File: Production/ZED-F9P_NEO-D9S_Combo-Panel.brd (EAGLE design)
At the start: 43.2 x 63.5 mm, 179 parts, among them J1 ANTENNA-SMA-GROUNDEDEDGE_SMA, J2 Qwiic Right Angle, J4 Qwiic Right Angle, U1 U-BLOX_NEO-D9S-00B, U2 3.3V, U4 U-BLOX_ZED-F9P, U5 ESD Diode, U6 ESD Diode, U7 BP2G1+_POWER_SPLITTER

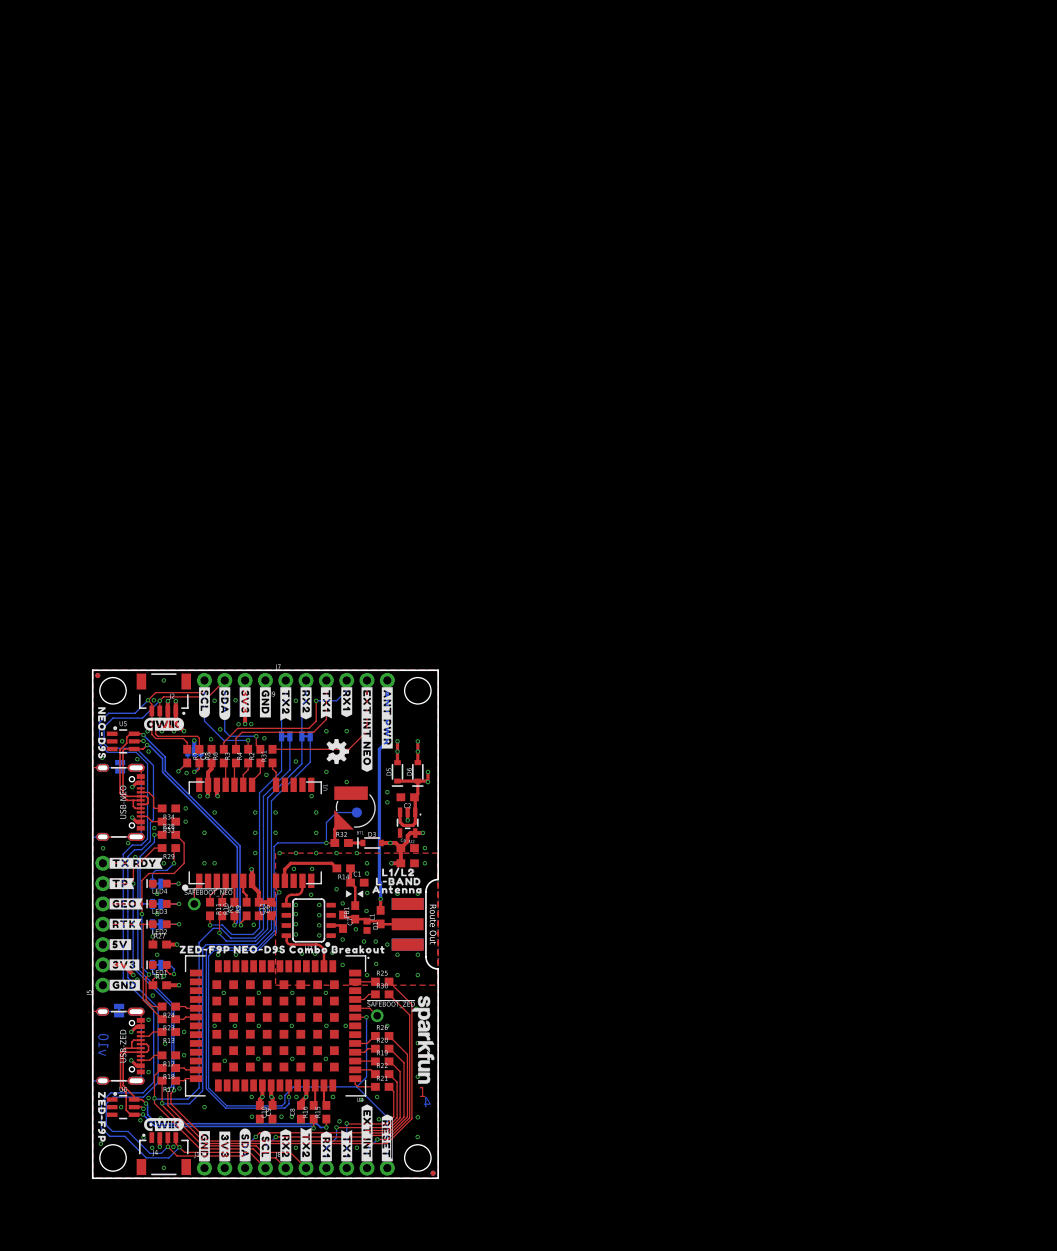
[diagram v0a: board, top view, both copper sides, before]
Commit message: Adds new panel
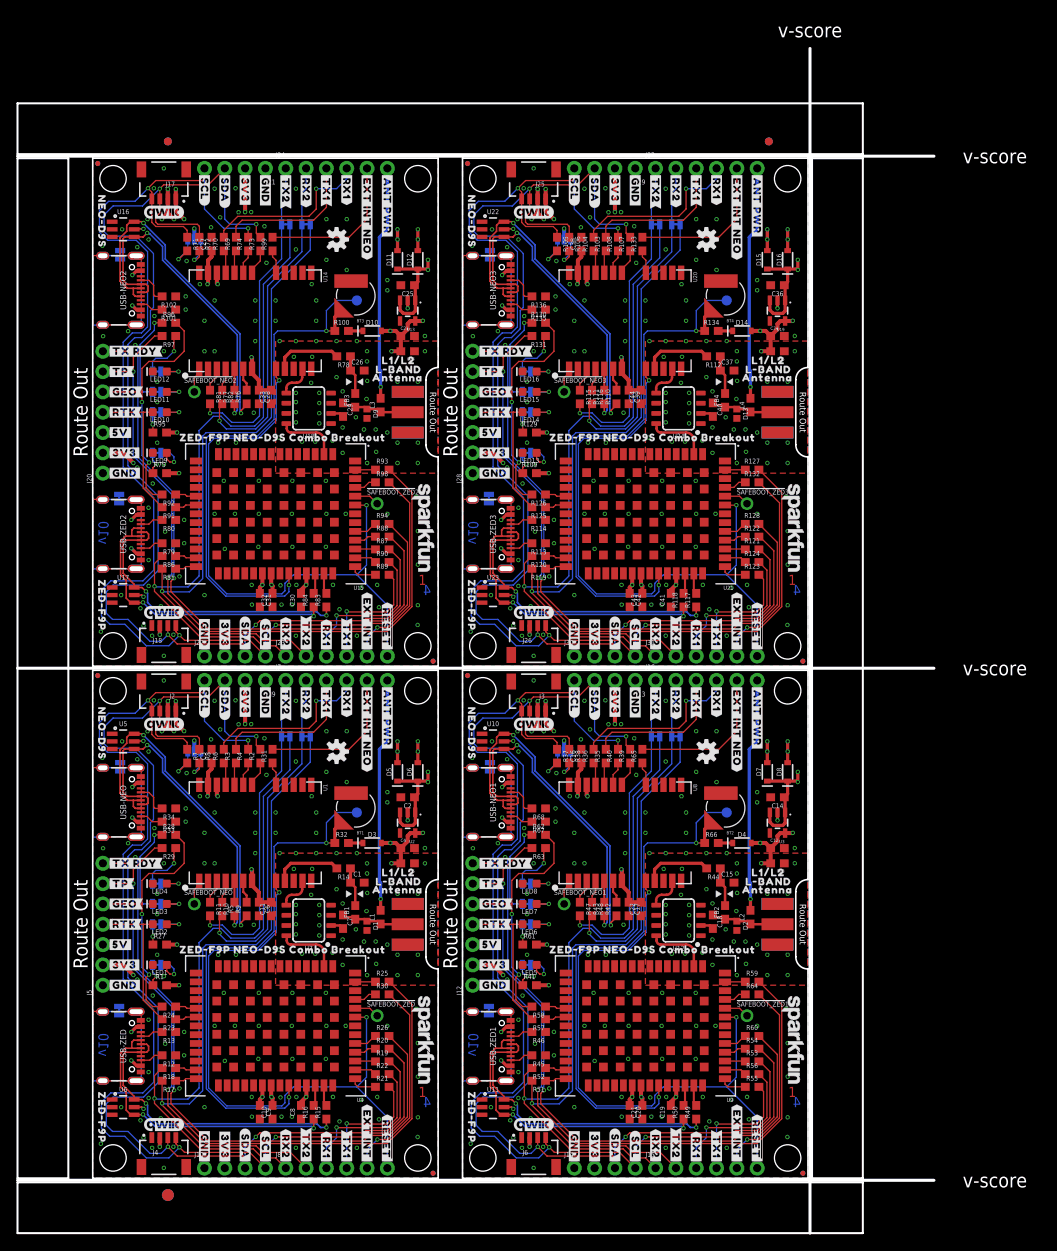
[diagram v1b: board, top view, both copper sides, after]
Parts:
- removed FRAME2: FRAME-LEDGER, SparkFun-Aesthetics:CREATIVE_COMMONS
- added !SAFEBOOT_NEO!1, !SAFEBOOT_NEO!2, !SAFEBOOT_NEO!3, !SAFEBOOT_ZED!1, !SAFEBOOT_ZED!2, !SAFEBOOT_ZED!3: TEST-POINTPOGO_PTH, SparkFun-Connectors:1X01_NO_SILK
- added BT2, BT3, BT4: RELOWABLE_BATTERY_MS421R, SparkFun-Batteries:MS421R_IV03E
- added C12, C14, C16, C17, C19, C20, C23, C25, C27, C28, C30, C31, C34, C36, C38, C39, C41, C42: 1.0uF, SparkFun-Capacitors:0603
- added C13, C21, C22, C24, C32, C33, C35, C43, C44: 0.1uF, SparkFun-Capacitors:0603
- added C15, C18, C26, C29, C37, C40: 47pF, SparkFun-Capacitors:0603
- added D10, D14, D4: 0.5A/40V/420mV, SparkFun-DiscreteSemi:SOD-323
- added D11, D12, D15, D16, D7, D8: 1A/23V/620mV, SparkFun-DiscreteSemi:SOD-323
- added D13, D2, D9: PESD0402-0402, SparkFun-DiscreteSemi:0402
- added E$1, E$2, E$3, E$4: (no value), SparkFun-Aesthetics:FIDUCIAL-1X2
- added E$5, E$6: (no value), SparkFun-Retired:FIDUCIAL-1.5X3
- added FB2, FB3, FB4: 30Ω/1.8A, SparkFun-Coils:0603
- added GEO1, GEO2, GEO3, PWR\1, PWR\2, PWR\3, RTK1, RTK2, RTK3, RX2-TX1, RX2-TX3, RX2-TX4, SHLD_NEO1, SHLD_NEO2, SHLD_NEO3, SHLD_ZED1, SHLD_ZED2, SHLD_ZED3, TP1, TP2, TP3, TX2-RX1, TX2-RX3, TX2-RX4: JUMPER-SMT_2_NC_TRACE_SILK, SparkFun-Jumpers:SMT-JUMPER_2_NC_TRACE_SILK
- added I2C1, I2C2, I2C3: JUMPER-SMT_3_NO_SILK, SparkFun-Jumpers:SMT-JUMPER_3_NO_SILK
- added J11, J19, J27: ANTENNA-SMA-GROUNDEDEDGE_SMA, SparkFun-RF:SMA-EDGE
- added J12, J20, J28: (no value), SparkFun-Connectors:1X07_NO_SILK
- added J13, J14, J21, J22, J29, J30: (no value), SparkFun-Connectors:1X04_NO_SILK
- added J15, J16, J23, J24, J31, J32: (no value), SparkFun-Connectors:1X06_NO_SILK
- added J17, J18, J25, J26, J3, J6: Qwiic Right Angle, SparkFun-Connectors:JST04_1MM_RA
- added JP1, JP10, JP15, JP16, JP17, JP18, JP2, JP24, JP25, JP7, JP8, JP9: STAND-OFF, SparkFun:STAND-OFF
- added JP11, JP12, JP13, JP14, JP19, JP20, JP22, JP23, JP3, JP4, JP5, JP6: FIDUCIALUFIDUCIAL, SparkFun:MICRO-FIDUCIAL
- added L2, L3, L4: DNP, SparkFun-Coils:0603_NO-CREAM
- added LED10, LED11, LED12, LED14, LED15, LED16, LED6, LED7, LED8: BLUE, SparkFun-LED:LED-0603
- added LED13, LED5, LED9: RED, SparkFun-LED:LED-0603
- added LOGO10, LOGO14, LOGO15, LOGO19, LOGO20, LOGO9: QWIIC_LOGO_5MM, SparkFun-Aesthetics:QWIIC_5MM
- added LOGO11, LOGO12, LOGO16, LOGO17, LOGO7: OSHW-LOGOS, SparkFun-Aesthetics:OSHW-LOGO-S
- added LOGO13, LOGO18, LOGO8: SFE_LOGO_NAME.1_INCH, SparkFun-Aesthetics:SFE_LOGO_NAME_.1
- added R100, R134, R66: 3.3k, SparkFun-Resistors:0603
- added R101, R102, R113, R114, R135, R136, R45, R46, R67, R68, R79, R80: 5.1k, SparkFun-Resistors:0603
- added R103, R104, R107, R108, R115, R116, R119, R120, R121, R122, R123, R124, R125, R126, R127, R128, R132, R133, R35, R36, R39, R40, R47, R48, R51, R52, R53, R54, R55, R56, R57, R58, R59, R60, R64, R65, R69, R70, R73, R74, R81, R82, R85, R86, R87, R88, R89, R90, R91, R92, R93, R94, R98, R99: 33, SparkFun-Resistors:0603
- added R105, R106, R37, R38, R71, R72: 2.2k, SparkFun-Resistors:0603
- added R109, R41, R75: 4.7k, SparkFun-Resistors:0603
- added R110, R111, R117, R118, R42, R43, R49, R50, R76, R77, R83, R84: 27, SparkFun-Resistors:0603
- added R112, R44, R78: 10, SparkFun-Resistors:0603
- added R129, R130, R131, R61, R62, R63, R95, R96, R97: 1k, SparkFun-Resistors:0603
- added U$100, U$180, U$260: (no value), output:#RTK#0
- added U$101, U$181, U$261: (no value), output:#RTK#1
- added U$102, U$182, U$262: (no value), output:#GEO#0
- added U$103, U$183, U$263: (no value), output:#GEO#1
- added U$104, U$184, U$264: (no value), output:#TP#0
- added U$105, U$185, U$265: (no value), output:#TP#1
- added U$106, U$186, U$266: (no value), output:#TX_RDY#0
- added U$107, U$187, U$267: (no value), output:#TX_RDY#1
- added U$108, U$109, U$135, U$188, U$189, U$215, U$268, U$269, U$295: (no value), output:#RX2#0
- added U$110, U$111, U$190, U$191, U$270, U$271: (no value), output:#RX2#3
- added U$112, U$113, U$134, U$192, U$193, U$214, U$272, U$273, U$294: (no value), output:#TX2#0
- added U$114, U$115, U$194, U$195, U$274, U$275: (no value), output:#TX2#3
- added U$116, U$117, U$196, U$197, U$276, U$277: (no value), output:#RX1#0
- added U$118, U$119, U$198, U$199, U$278, U$279: (no value), output:#RX1#2
- added U$120, U$121, U$200, U$201, U$280, U$281: (no value), output:#TX1#0
- added U$122, U$123, U$202, U$203, U$282, U$283: (no value), output:#TX1#2
- added U$124, U$204, U$284: (no value), output:#EXT_INT_NEO#0
- added U$125, U$205, U$285: (no value), output:#EXT_INT_NEO#1
- added U$126, U$127, U$206, U$207, U$286, U$287: (no value), output:#SDA#0
- added U$128, U$129, U$208, U$209, U$288, U$289: (no value), output:#SDA#1
- added U$130, U$131, U$210, U$211, U$290, U$291: (no value), output:#SCL#0
- added U$132, U$133, U$212, U$213, U$292, U$293: (no value), output:#SCL#1
- added U$136, U$216, U$296: (no value), output:ZED#F9P10
- added U$137, U$217, U$297: (no value), output:NEO#D9S10
- added U$138, U$218, U$298: (no value), output:#PWR#0
- added U$139, U$171, U$172, U$219, U$251, U$252, U$299, U$91, U$92: (no value), output:#3V3#4
- added U$140, U$220, U$300: (no value), output:#EXT_INT_ZED#0
- added U$141, U$221, U$301: (no value), output:ZED#F9P_NEO#D9S_COMBO_BREAKOUT0
- added U$142, U$222, U$302: (no value), top:##SAFEBOOT#_NEO#13
- added U$143, U$223, U$303: (no value), top:##SAFEBOOT#_ZED#14
- added U$144, U$224, U$304: (no value), top:#SHLD_ZED#15
- added U$145, U$225, U$305: (no value), top:#SHLD_NEO#12
- added U$146, U$226, U$306: (no value), top:ZED#F9P16
- added U$147, U$227, U$307: (no value), top:NEO#D9S16
- added U$148, U$228, U$308: (no value), top:COMBO16
- added U$149, U$229, U$309: (no value), top:BREAKOUT17
- added U$150, U$230, U$310: (no value), SparkFun-Aesthetics:SFE_LOGO_NAME_.2
- added U$151, U$231, U$311: (no value), top:L1#L218
- added U$152, U$232, U$312: (no value), top:ANTENNA18
- added U$153, U$233, U$313: (no value), top:L#BAND18
- added U$154, U$234, U$314: (no value), top:OPEN_JUMPERS13
- added U$155, U$235, U$315: (no value), top:TO_ISOLATE_UART214
- added U$156, U$236, U$316: (no value), top:DEF_ADDRESS#_12
- added U$157, U$237, U$317: (no value), top:NEO#D9S#13
- added U$158, U$238, U$318: (no value), top:ZED#F9P#13
- added U$159, U$239, U$319: (no value), top:0X4313
- added U$160, U$240, U$320: (no value), top:0X4213
- added U$161, U$162, U$163, U$241, U$242, U$243, U$38, U$77, U$83: (no value), output:#GND#0
- added U$164, U$165, U$166, U$244, U$245, U$246, U$84, U$85, U$86: (no value), output:#GND#1
- added U$167, U$247, U$87: (no value), output:#5V#0
- added U$168, U$248, U$88: (no value), output:#5V#6
- added U$169, U$170, U$177, U$249, U$250, U$257, U$89, U$90, U$97: (no value), output:#3V3#0
- added U$173, U$253, U$93: (no value), output:##RESET##0
- added U$174, U$254, U$94: (no value), output:##RESET##1
- added U$175, U$255, U$95: (no value), output:#EXT_INT#0
- added U$176, U$256, U$96: (no value), output:#I�C#0
- added U$178, U$258, U$98: (no value), output:#ANT_PWR#0
- added U$179, U$259, U$99: (no value), output:#ANT_PWR#1
- added U10, U11, U16, U17, U22, U23: ESD Diode, SparkFun-DiscreteSemi:SOT-23-6
- added U12, U18, U24: BP2G1+_POWER_SPLITTER, SparkFun-RF:XX21
- added U13, U19, U3: 3.3V, SparkFun-IC-Power:SOT23-5
- added U14, U20, U8: U-BLOX_NEO-D9S-00B, SparkFun-GPS:NEO-M9N/M8T/M8U/D9S
- added U15, U21, U9: U-BLOX_ZED-F9P, SparkFun-GPS:ZED-F9P
- added USB-NEO1, USB-NEO2, USB-NEO3, USB-ZED1, USB-ZED2, USB-ZED3: USB Female Type C Connector, SparkFun-Connectors:USB-C-16P_4LAYER-PADS
- added V_BKCP1, V_BKCP2, V_BKCP3: TEST-POINT3X5, SparkFun-Connectors:PAD.03X.05
- LOGO5: value SPECIAL_INSTRUCTIONS-ORDERING -> OSHW-LOGOS; device SparkFun-Aesthetics:ORDERING_INSTRUCTIONS -> SparkFun-Aesthetics:OSHW-LOGO-S
- moved LOGO5 61.0 mm to (52.3, 2.54), flipped to the bottom, turned to 90 degrees
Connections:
- new net !RESET!1: J15.6, U8.8, U9.49
- new net !RESET!2: J23.6, U14.8, U15.49
- new net !RESET!3: J31.6, U20.8, U21.49
- new net !SAFEBOOT_NEO!1: !SAFEBOOT_NEO!1.1, U8.1
- new net !SAFEBOOT_NEO!2: !SAFEBOOT_NEO!2.1, U14.1
- new net !SAFEBOOT_NEO!3: !SAFEBOOT_NEO!3.1, U20.1
- new net !SAFEBOOT_ZED!1: !SAFEBOOT_ZED!1.1, U9.50
- new net !SAFEBOOT_ZED!2: !SAFEBOOT_ZED!2.1, U15.50
- new net !SAFEBOOT_ZED!3: !SAFEBOOT_ZED!3.1, U21.50
- new net 3.3V1: C12.1, C13.2, C16.1, C17.1, C19.2, C20.1, C21.2, C22.2, D4.A, I2C1.2, J12.2, J13.2, J14.2, J3.2, J6.2, R41.2, R61.2, U3.5, U8.22, U8.23, U8.7, U9.33, U9.34, U9.38
- new net 3.3V2: C23.1, C24.2, C27.1, C28.1, C30.2, C31.1, C32.2, C33.2, D10.A, I2C2.2, J17.2, J18.2, J20.2, J21.2, J22.2, R75.2, R95.2, U13.5, U14.22, U14.23, U14.7, U15.33, U15.34, U15.38
- new net 3.3V3: C34.1, C35.2, C38.1, C39.1, C41.2, C42.1, C43.2, C44.2, D14.A, I2C3.2, J25.2, J26.2, J28.2, J29.2, J30.2, R109.2, R129.2, U19.5, U20.22, U20.23, U20.7, U21.33, U21.34, U21.38
- new net 5V1: C14.1, D7.C, D8.C, J12.3, U3.1, U3.3
- new net 5V2: C25.1, D11.C, D12.C, J20.3, U13.1, U13.3
- new net 5V3: C36.1, D15.C, D16.C, J28.3, U19.1, U19.3
- new net ANT1: C18.2, U12.2
- new net ANT2: C29.2, U18.2
- new net ANT3: C40.2, U24.2
- new net ANT_NEO1: U12.5, U8.11
- new net ANT_NEO2: U14.11, U18.5
- new net ANT_NEO3: U20.11, U24.5
- new net ANT_PWR1: J16.6, L2.2
- new net ANT_PWR2: J24.6, L3.2
- new net ANT_PWR3: J32.6, L4.2
- new net ANT_VCC1: C15.1, FB2.2, R44.1
- new net ANT_VCC2: C26.1, FB3.2, R78.1
- new net ANT_VCC3: C37.1, FB4.2, R112.1
- new net ANT_ZED1: U12.8, U9.2
- new net ANT_ZED2: U15.2, U18.8
- new net ANT_ZED3: U21.2, U24.8
- new net D+_NEO1: R42.1, U10.6, USB-NEO1.A6, USB-NEO1.B6
- new net D+_NEO2: R76.1, U16.6, USB-NEO2.A6, USB-NEO2.B6
- new net D+_NEO3: R110.1, U22.6, USB-NEO3.A6, USB-NEO3.B6
- new net D+_ZED1: R49.1, U11.6, USB-ZED1.A6, USB-ZED1.B6
- new net D+_ZED2: R83.1, U17.6, USB-ZED2.A6, USB-ZED2.B6
- new net D+_ZED3: R117.1, U23.6, USB-ZED3.A6, USB-ZED3.B6
- new net D-_NEO1: R43.1, U10.4, USB-NEO1.A7, USB-NEO1.B7
- new net D-_NEO2: R77.1, U16.4, USB-NEO2.A7, USB-NEO2.B7
- new net D-_NEO3: R111.1, U22.4, USB-NEO3.A7, USB-NEO3.B7
- new net D-_ZED1: R50.1, U11.4, USB-ZED1.A7, USB-ZED1.B7
- new net D-_ZED2: R84.1, U17.4, USB-ZED2.A7, USB-ZED2.B7
- new net D-_ZED3: R118.1, U23.4, USB-ZED3.A7, USB-ZED3.B7
- new net EXT_INT_NEO1: J16.5, R65.2
- new net EXT_INT_NEO2: J24.5, R99.2
- new net EXT_INT_NEO3: J32.5, R133.2
- new net EXT_INT_ZED1: J15.5, R64.2
- new net EXT_INT_ZED2: J23.5, R98.2
- new net EXT_INT_ZED3: J31.5, R132.2
- new net GEO1: J12.5, R58.2, R62.2
- new net GEO2: J20.5, R92.2, R96.2
- new net GEO3: J28.5, R126.2, R130.2
- new net GND1: BT2.-, C12.2, C13.1, C14.2, C15.2, C16.2, C17.2, C19.1, C20.2, C21.1, C22.1, D2.2, J11.GND@0, J11.GND@1, J11.GND@2, J11.GND@3, J12.1, J13.1, J14.1, J3.1, J6.1, LED5.C, LED7.C, LED8.C, R45.1, R46.1, R67.1, R68.1, SHLD_NEO1.1, SHLD_ZED1.1, U10.2, U11.2, U12.1, U12.3, U12.4, U12.6, U12.7, U3.2, U8.10, U8.12, U8.13, U8.24, U9.1, U9.100, U9.101, U9.102, U9.12, U9.14, U9.3, U9.32, U9.37, U9.41, U9.48, U9.55, U9.56, U9.57, U9.58, U9.59, U9.60, U9.61, U9.62, U9.63, U9.64, U9.65, U9.66, U9.67, U9.68, U9.69, U9.70, U9.71, U9.72, U9.73, U9.74, U9.75, U9.76, U9.77, U9.78, U9.79, U9.80, U9.81, U9.82, U9.83, U9.84, U9.85, U9.86, U9.87, U9.88, U9.89, U9.90, U9.91, U9.92, U9.93, U9.94, U9.95, U9.96, U9.97, U9.98, U9.99, USB-NEO1.GND, USB-NEO1.GND2, USB-ZED1.GND, USB-ZED1.GND2
- new net GND2: BT3.-, C23.2, C24.1, C25.2, C26.2, C27.2, C28.2, C30.1, C31.2, C32.1, C33.1, D9.2, J17.1, J18.1, J19.GND@0, J19.GND@1, J19.GND@2, J19.GND@3, J20.1, J21.1, J22.1, LED11.C, LED12.C, LED9.C, R101.1, R102.1, R79.1, R80.1, SHLD_NEO2.1, SHLD_ZED2.1, U13.2, U14.10, U14.12, U14.13, U14.24, U15.1, U15.100, U15.101, U15.102, U15.12, U15.14, U15.3, U15.32, U15.37, U15.41, U15.48, U15.55, U15.56, U15.57, U15.58, U15.59, U15.60, U15.61, U15.62, U15.63, U15.64, U15.65, U15.66, U15.67, U15.68, U15.69, U15.70, U15.71, U15.72, U15.73, U15.74, U15.75, U15.76, U15.77, U15.78, U15.79, U15.80, U15.81, U15.82, U15.83, U15.84, U15.85, U15.86, U15.87, U15.88, U15.89, U15.90, U15.91, U15.92, U15.93, U15.94, U15.95, U15.96, U15.97, U15.98, U15.99, U16.2, U17.2, U18.1, U18.3, U18.4, U18.6, U18.7, USB-NEO2.GND, USB-NEO2.GND2, USB-ZED2.GND, USB-ZED2.GND2
- new net GND3: BT4.-, C34.2, C35.1, C36.2, C37.2, C38.2, C39.2, C41.1, C42.2, C43.1, C44.1, D13.2, J25.1, J26.1, J27.GND@0, J27.GND@1, J27.GND@2, J27.GND@3, J28.1, J29.1, J30.1, LED13.C, LED15.C, LED16.C, R113.1, R114.1, R135.1, R136.1, SHLD_NEO3.1, SHLD_ZED3.1, U19.2, U20.10, U20.12, U20.13, U20.24, U21.1, U21.100, U21.101, U21.102, U21.12, U21.14, U21.3, U21.32, U21.37, U21.41, U21.48, U21.55, U21.56, U21.57, U21.58, U21.59, U21.60, U21.61, U21.62, U21.63, U21.64, U21.65, U21.66, U21.67, U21.68, U21.69, U21.70, U21.71, U21.72, U21.73, U21.74, U21.75, U21.76, U21.77, U21.78, U21.79, U21.80, U21.81, U21.82, U21.83, U21.84, U21.85, U21.86, U21.87, U21.88, U21.89, U21.90, U21.91, U21.92, U21.93, U21.94, U21.95, U21.96, U21.97, U21.98, U21.99, U22.2, U23.2, U24.1, U24.3, U24.4, U24.6, U24.7, USB-NEO3.GND, USB-NEO3.GND2, USB-ZED3.GND, USB-ZED3.GND2
- new net N$100: GEO2.2, R96.1
- new net N$101: R97.1, TP2.2
- new net N$102: R91.1, U15.20
- new net N$103: R92.1, U15.19
- new net N$104: R93.1, U15.53
- new net N$105: R98.1, U15.51
- new net N$106: R99.1, U14.17
- new net N$107: D10.C, R100.2
- new net N$108: R101.2, USB-NEO2.B5
- new net N$109: R102.2, USB-NEO2.A5
- new net N$110: PWR\2.2, R75.1
- new net N$111: LED9.A, PWR\2.1
- new net N$112: I2C3.1, R106.2
- new net N$113: I2C3.3, R105.2
- new net N$114: R110.2, U20.6
- new net N$115: R111.2, U20.5
- new net N$116: R113.2, USB-ZED3.B5
- new net N$117: R114.2, USB-ZED3.A5
- new net N$118: R115.1, U20.3
- new net N$119: R116.1, U20.4
- new net N$120: R103.1, U20.20
- new net N$121: R104.1, U20.21
- new net N$122: R107.1, U20.18
- new net N$123: R108.1, U20.19
- new net N$124: R117.2, U21.40
- new net N$125: R118.2, U21.39
- new net N$126: R121.1, U21.44
- new net N$127: R122.1, U21.45
- new net N$128: R123.1, U21.42
- new net N$129: R124.1, U21.43
- new net N$130: R119.1, U21.27
- new net N$131: R120.1, U21.26
- new net N$132: R128.1, U21.46
- new net N$133: LED14.A, RTK3.1
- new net N$134: GEO3.1, LED15.A
- new net N$135: LED16.A, TP3.1
- new net N$136: R129.1, RTK3.2
- new net N$137: GEO3.2, R130.1
- new net N$138: R131.1, TP3.2
- new net N$139: R125.1, U21.20
- new net N$140: R126.1, U21.19
- new net N$141: R127.1, U21.53
- new net N$142: R132.1, U21.51
- new net N$143: R133.1, U20.17
- new net N$144: D14.C, R134.2
- new net N$145: R135.2, USB-NEO3.B5
- new net N$146: R136.2, USB-NEO3.A5
- new net N$147: PWR\3.2, R109.1
- new net N$148: LED13.A, PWR\3.1
- new net N$38: I2C1.1, R38.2
- new net N$39: I2C1.3, R37.2
- new net N$40: R42.2, U8.6
- new net N$41: R43.2, U8.5
- new net N$42: R45.2, USB-ZED1.B5
- new net N$43: R46.2, USB-ZED1.A5
- new net N$44: R47.1, U8.3
- new net N$45: R48.1, U8.4
- new net N$46: R35.1, U8.20
- new net N$47: R36.1, U8.21
- new net N$48: R39.1, U8.18
- new net N$49: R40.1, U8.19
- new net N$50: R49.2, U9.40
- new net N$51: R50.2, U9.39
- new net N$52: R53.1, U9.44
- new net N$53: R54.1, U9.45
- new net N$54: R55.1, U9.42
- new net N$55: R56.1, U9.43
- new net N$56: R51.1, U9.27
- new net N$57: R52.1, U9.26
- new net N$58: R60.1, U9.46
- new net N$59: LED6.A, RTK1.1
- new net N$60: GEO1.1, LED7.A
- new net N$61: LED8.A, TP1.1
- new net N$62: R61.1, RTK1.2
- new net N$63: GEO1.2, R62.1
- new net N$64: R63.1, TP1.2
- new net N$65: R57.1, U9.20
- new net N$66: R58.1, U9.19
- new net N$67: R59.1, U9.53
- new net N$68: R64.1, U9.51
- new net N$69: R65.1, U8.17
- new net N$70: D4.C, R66.2
- new net N$71: R67.2, USB-NEO1.B5
- new net N$72: R68.2, USB-NEO1.A5
- new net N$73: PWR\1.2, R41.1
- new net N$74: LED5.A, PWR\1.1
- new net N$75: I2C2.1, R72.2
- new net N$76: I2C2.3, R71.2
- new net N$77: R76.2, U14.6
- new net N$78: R77.2, U14.5
- new net N$79: R79.2, USB-ZED2.B5
- new net N$80: R80.2, USB-ZED2.A5
- new net N$81: R81.1, U14.3
- new net N$82: R82.1, U14.4
- new net N$83: R69.1, U14.20
- new net N$84: R70.1, U14.21
- new net N$85: R73.1, U14.18
- new net N$86: R74.1, U14.19
- new net N$87: R83.2, U15.40
- new net N$88: R84.2, U15.39
- new net N$89: R87.1, U15.44
- new net N$90: R88.1, U15.45
- new net N$91: R89.1, U15.42
- new net N$92: R90.1, U15.43
- new net N$93: R85.1, U15.27
- new net N$94: R86.1, U15.26
- new net N$95: R94.1, U15.46
- new net N$96: LED10.A, RTK2.1
- new net N$97: GEO2.1, LED11.A
- new net N$98: LED12.A, TP2.1
- new net N$99: R95.1, RTK2.2
- new net RTK1: J12.4, LED6.C, R57.2
- new net RTK2: J20.4, LED10.C, R91.2
- new net RTK3: J28.4, LED14.C, R125.2
- new net RXD1_NEO1: J16.4, R36.2
- new net RXD1_NEO2: J24.4, R70.2
- new net RXD1_NEO3: J32.4, R104.2
- new net RXD1_ZED1: J15.3, R56.2
- new net RXD1_ZED2: J23.3, R90.2
- new net RXD1_ZED3: J31.3, R124.2
- new net RXD2_NEO1: J16.2, R48.2, TX2-RX1.2
- new net RXD2_NEO2: J24.2, R82.2, TX2-RX3.2
- new net RXD2_NEO3: J32.2, R116.2, TX2-RX4.2
- new net RXD2_ZED1: J15.1, R52.2, RX2-TX1.1
- new net RXD2_ZED2: J23.1, R86.2, RX2-TX3.1
- new net RXD2_ZED3: J31.1, R120.2, RX2-TX4.1
- new net SCL1: J13.4, J14.4, J3.4, J6.4, R37.1, R40.2, R54.2
- new net SCL2: J17.4, J18.4, J21.4, J22.4, R71.1, R74.2, R88.2
- new net SCL3: J25.4, J26.4, J29.4, J30.4, R105.1, R108.2, R122.2
- new net SDA1: J13.3, J14.3, J3.3, J6.3, R38.1, R39.2, R53.2
- new net SDA2: J17.3, J18.3, J21.3, J22.3, R72.1, R73.2, R87.2
- new net SDA3: J25.3, J26.3, J29.3, J30.3, R106.1, R107.2, R121.2
- new net SHIELD_NEO1: SHLD_NEO1.2, USB-NEO1.SHLD1, USB-NEO1.SHLD2, USB-NEO1.SHLD3, USB-NEO1.SHLD4
- new net SHIELD_NEO2: SHLD_NEO2.2, USB-NEO2.SHLD1, USB-NEO2.SHLD2, USB-NEO2.SHLD3, USB-NEO2.SHLD4
- new net SHIELD_NEO3: SHLD_NEO3.2, USB-NEO3.SHLD1, USB-NEO3.SHLD2, USB-NEO3.SHLD3, USB-NEO3.SHLD4
- new net SHIELD_ZED1: SHLD_ZED1.2, USB-ZED1.SHLD1, USB-ZED1.SHLD2, USB-ZED1.SHLD3, USB-ZED1.SHLD4
- new net SHIELD_ZED2: SHLD_ZED2.2, USB-ZED2.SHLD1, USB-ZED2.SHLD2, USB-ZED2.SHLD3, USB-ZED2.SHLD4
- new net SHIELD_ZED3: SHLD_ZED3.2, USB-ZED3.SHLD1, USB-ZED3.SHLD2, USB-ZED3.SHLD3, USB-ZED3.SHLD4
- new net SMA1: C18.1, D2.1, FB2.1, J11.SIG, L2.1
- new net SMA2: C29.1, D9.1, FB3.1, J19.SIG, L3.1
- new net SMA3: C40.1, D13.1, FB4.1, J27.SIG, L4.1
- new net TP1: J12.6, R59.2, R63.2
- new net TP2: J20.6, R93.2, R97.2
- new net TP3: J28.6, R127.2, R131.2
- new net TXD1_NEO1: J16.3, R35.2
- new net TXD1_NEO2: J24.3, R69.2
- new net TXD1_NEO3: J32.3, R103.2
- new net TXD1_ZED1: J15.4, R55.2
- new net TXD1_ZED2: J23.4, R89.2
- new net TXD1_ZED3: J31.4, R123.2
- new net TXD2_NEO1: J16.1, R47.2, RX2-TX1.2
- new net TXD2_NEO2: J24.1, R81.2, RX2-TX3.2
- new net TXD2_NEO3: J32.1, R115.2, RX2-TX4.2
- new net TXD2_ZED1: J15.2, R51.2, TX2-RX1.1
- new net TXD2_ZED2: J23.2, R85.2, TX2-RX3.1
- new net TXD2_ZED3: J31.2, R119.2, TX2-RX4.1
- new net TX_RDY1: J12.7, R60.2
- new net TX_RDY2: J20.7, R94.2
- new net TX_RDY3: J28.7, R128.2
- new net VCC_RF1: R44.2, U8.9
- new net VCC_RF2: R78.2, U14.9
- new net VCC_RF3: R112.2, U20.9
- new net V_BKCP1: BT2.+, R66.1, U9.36, V_BKCP1.1
- new net V_BKCP2: BT3.+, R100.1, U15.36, V_BKCP2.1
- new net V_BKCP3: BT4.+, R134.1, U21.36, V_BKCP3.1
- new net V_USB1: D7.A, U11.5, USB-ZED1.VBUS1, USB-ZED1.VBUS2
- new net V_USB2: D11.A, U17.5, USB-ZED2.VBUS1, USB-ZED2.VBUS2
- new net V_USB3: D15.A, U23.5, USB-ZED3.VBUS1, USB-ZED3.VBUS2
- new net V_USB_1: D8.A, U10.5, USB-NEO1.VBUS1, USB-NEO1.VBUS2
- new net V_USB_3: D12.A, U16.5, USB-NEO2.VBUS1, USB-NEO2.VBUS2
- new net V_USB_4: D16.A, U22.5, USB-NEO3.VBUS1, USB-NEO3.VBUS2
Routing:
- net SCL1: track 0.00 -> 158.6 mm, vias 0 -> 4
- net SCL2: track 0.00 -> 158.6 mm, vias 0 -> 4
- net SCL3: track 0.00 -> 158.6 mm, vias 0 -> 4
- net SDA3: track 0.00 -> 157.3 mm, vias 0 -> 4
- net SDA2: track 0.00 -> 157.3 mm, vias 0 -> 4
- net SDA1: track 0.00 -> 157.3 mm, vias 0 -> 4
- net V_USB1: track 0.00 -> 94.3 mm, vias 0 -> 5
- net V_USB3: track 0.00 -> 94.3 mm, vias 0 -> 5
- net V_USB2: track 0.00 -> 94.3 mm, vias 0 -> 5
- net TP1: track 0.00 -> 92.3 mm, vias 0 -> 2
- net TP3: track 0.00 -> 92.3 mm, vias 0 -> 2
- net TP2: track 0.00 -> 92.3 mm, vias 0 -> 2
- net 5V3: track 0.00 -> 91.5 mm, vias 0 -> 2
- net 5V2: track 0.00 -> 91.5 mm, vias 0 -> 2
- net 5V1: track 0.00 -> 91.5 mm, vias 0 -> 2
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- added copper zone on layer 15, net 3.3V1
- added copper zone on layer 15, net 3.3V2
- added copper zone on layer 15, net 3.3V3
- added copper zone on layer 1, net GND1
- added copper zone on layer 16, net GND1
- added copper zone on layer 2, net GND1
- added copper zone on layer 1, net GND2
- added copper zone on layer 16, net GND2
- added copper zone on layer 2, net GND2
- added copper zone on layer 1, net GND3
- added copper zone on layer 16, net GND3
- added copper zone on layer 2, net GND3
- added copper zone on layer 1, net SHIELD_NEO1
- added copper zone on layer 16, net SHIELD_NEO1
- added copper zone on layer 1, net SHIELD_NEO2
- added copper zone on layer 16, net SHIELD_NEO2
- added copper zone on layer 1, net SHIELD_NEO3
- added copper zone on layer 16, net SHIELD_NEO3
- added copper zone on layer 1, net SHIELD_ZED1
- added copper zone on layer 16, net SHIELD_ZED1
- added copper zone on layer 1, net SHIELD_ZED2
- added copper zone on layer 16, net SHIELD_ZED2
- added copper zone on layer 1, net SHIELD_ZED3
- added copper zone on layer 16, net SHIELD_ZED3
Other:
- board size 43.2 x 63.5 mm -> 114.6 x 148.1 mm
- board text added: "v-score"
- board text removed: "1.6mm Thickness 4-Layers 1oz Copper 0.5oz Inner Copper Stackup: JLC7628 Material: TG135-140 Lead-Free HASL finish Red soldermask White silkscreen"
- board text removed: "Measurements in inches"
- board text removed: "Paul Clark"
- board text removed: "Revised By: Elias Santistevan"

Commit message: Adds new panel - bottom silk change
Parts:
- moved U$238 0.25 mm to (6.60, 115.2)
- moved U$240 0.25 mm to (6.60, 120.8)
- moved U$80 0.25 mm to (6.60, 51.2)
- moved U$82 0.25 mm to (6.60, 56.8)
- moved U$236 0.25 mm to (9.14, 117.3)
- moved U$237 0.25 mm to (7.87, 115.1)
- moved U$239 0.25 mm to (7.87, 120.8)
- moved U$76 0.25 mm to (9.14, 53.3)
- moved U$79 0.25 mm to (7.87, 51.1)
- moved U$81 0.25 mm to (7.87, 56.8)
- moved U$156 0.25 mm to (55.4, 53.3)
- moved U$157 0.25 mm to (54.1, 51.1)
- moved U$158 0.25 mm to (52.8, 51.2)
- moved U$159 0.25 mm to (54.1, 56.8)
- moved U$160 0.25 mm to (52.8, 56.8)
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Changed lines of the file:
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@@
 <layers>
 <layer number="1" name="Top" color="4" fill="1" visible="yes" active="yes"/>
+<layer number="2" name="Route2" color="16" fill="1" visible="no" active="yes"/>
+<layer number="15" name="Route15" color="23" fill="1" visible="no" active="yes"/>
 <layer number="16" name="Bottom" color="1" fill="1" visible="yes" active="yes"/>
 <layer number="17" name="Pads" color="2" fill="1" visible="yes" active="yes"/>
@@
 <element name="U$73" library="top" package="OPEN_JUMPERS13" value="" x="22.225" y="50.927" smashed="yes" rot="MR90"/>
 <element name="U$74" library="top" package="TO_ISOLATE_UART214" value="" x="20.828" y="50.927" smashed="yes" rot="MR90"/>
-<element name="U$76" library="top" package="DEF_ADDRESS#_12" value="" x="8.89" y="53.34" smashed="yes" rot="MR90"/>
-<element name="U$79" library="top" package="NEO#D9S#13" value="" x="7.62" y="51.054" smashed="yes" rot="MR90"/>
-<element name="U$80" library="top" package="ZED#F9P#13" value="" x="6.35" y="51.181" smashed="yes" rot="MR90"/>
-<element name="U$81" library="top" package="0X4313" value="" x="7.62" y="56.769" smashed="yes" rot="MR90"/>
-<element name="U$82" library="top" package="0X4213" value="" x="6.35" y="56.769" smashed="yes" rot="MR90"/>
+<element name="U$76" library="top" package="DEF_ADDRESS#_12" value="" x="9.144" y="53.34" smashed="yes" rot="MR90"/>
+<element name="U$79" library="top" package="NEO#D9S#13" value="" x="7.874" y="51.054" smashed="yes" rot="MR90"/>
+<element name="U$80" library="top" package="ZED#F9P#13" value="" x="6.604" y="51.181" smashed="yes" rot="MR90"/>
+<element name="U$81" library="top" package="0X4313" value="" x="7.874" y="56.769" smashed="yes" rot="MR90"/>
+<element name="U$82" library="top" package="0X4213" value="" x="6.604" y="56.769" smashed="yes" rot="MR90"/>
 <element name="LOGO6" library="SparkFun-Aesthetics" package="QWIIC_5MM" value="QWIIC_LOGO_5MM" x="8.89" y="56.769" smashed="yes"/>
 <element name="JP1" library="SparkFun" package="STAND-OFF" value="STAND-OFF" x="48.768" y="60.9346" smashed="yes"/>
@@
 <element name="U$154" library="top" package="OPEN_JUMPERS13" value="" x="68.453" y="50.927" smashed="yes" rot="MR90"/>
 <element name="U$155" library="top" package="TO_ISOLATE_UART214" value="" x="67.056" y="50.927" smashed="yes" rot="MR90"/>
-<element name="U$156" library="top" package="DEF_ADDRESS#_12" value="" x="55.118" y="53.34" smashed="yes" rot="MR90"/>
-<element name="U$157" library="top" package="NEO#D9S#13" value="" x="53.848" y="51.054" smashed="yes" rot="MR90"/>
-<element name="U$158" library="top" package="ZED#F9P#13" value="" x="52.578" y="51.181" smashed="yes" rot="MR90"/>
-<element name="U$159" library="top" package="0X4313" value="" x="53.848" y="56.769" smashed="yes" rot="MR90"/>
-<element name="U$160" library="top" package="0X4213" value="" x="52.578" y="56.769" smashed="yes" rot="MR90"/>
+<element name="U$156" library="top" package="DEF_ADDRESS#_12" value="" x="55.372" y="53.34" smashed="yes" rot="MR90"/>
+<element name="U$157" library="top" package="NEO#D9S#13" value="" x="54.102" y="51.054" smashed="yes" rot="MR90"/>
+<element name="U$158" library="top" package="ZED#F9P#13" value="" x="52.832" y="51.181" smashed="yes" rot="MR90"/>
+<element name="U$159" library="top" package="0X4313" value="" x="54.102" y="56.769" smashed="yes" rot="MR90"/>
+<element name="U$160" library="top" package="0X4213" value="" x="52.832" y="56.769" smashed="yes" rot="MR90"/>
 <element name="LOGO10" library="SparkFun-Aesthetics" package="QWIIC_5MM" value="QWIIC_LOGO_5MM" x="55.118" y="56.769" smashed="yes"/>
 <element name="JP9" library="SparkFun" package="STAND-OFF" value="STAND-OFF" x="2.54" y="124.9426" smashed="yes"/>
@@
 <element name="U$234" library="top" package="OPEN_JUMPERS13" value="" x="22.225" y="114.935" smashed="yes" rot="MR90"/>
 <element name="U$235" library="top" package="TO_ISOLATE_UART214" value="" x="20.828" y="114.935" smashed="yes" rot="MR90"/>
-<element name="U$236" library="top" package="DEF_ADDRESS#_12" value="" x="8.89" y="117.348" smashed="yes" rot="MR90"/>
-<element name="U$237" library="top" package="NEO#D9S#13" value="" x="7.62" y="115.062" smashed="yes" rot="MR90"/>
-<element name="U$238" library="top" package="ZED#F9P#13" value="" x="6.35" y="115.189" smashed="yes" rot="MR90"/>
-<element name="U$239" library="top" package="0X4313" value="" x="7.62" y="120.777" smashed="yes" rot="MR90"/>
-<element name="U$240" library="top" package="0X4213" value="" x="6.35" y="120.777" smashed="yes" rot="MR90"/>
+<element name="U$236" library="top" package="DEF_ADDRESS#_12" value="" x="9.144" y="117.348" smashed="yes" rot="MR90"/>
+<element name="U$237" library="top" package="NEO#D9S#13" value="" x="7.874" y="115.062" smashed="yes" rot="MR90"/>
+<element name="U$238" library="top" package="ZED#F9P#13" value="" x="6.604" y="115.189" smashed="yes" rot="MR90"/>
+<element name="U$239" library="top" package="0X4313" value="" x="7.874" y="120.777" smashed="yes" rot="MR90"/>
+<element name="U$240" library="top" package="0X4213" value="" x="6.604" y="120.777" smashed="yes" rot="MR90"/>
 <element name="LOGO15" library="SparkFun-Aesthetics" package="QWIIC_5MM" value="QWIIC_LOGO_5MM" x="8.89" y="120.777" smashed="yes"/>
 <element name="JP17" library="SparkFun" package="STAND-OFF" value="STAND-OFF" x="48.768" y="124.9426" smashed="yes"/>
@@
 <element name="U$314" library="top" package="OPEN_JUMPERS13" value="" x="68.453" y="114.935" smashed="yes" rot="MR90"/>
 <element name="U$315" library="top" package="TO_ISOLATE_UART214" value="" x="67.056" y="114.935" smashed="yes" rot="MR90"/>
-<element name="U$316" library="top" package="DEF_ADDRESS#_12" value="" x="55.118" y="117.348" smashed="yes" rot="MR90"/>
-<element name="U$317" library="top" package="NEO#D9S#13" value="" x="53.848" y="115.062" smashed="yes" rot="MR90"/>
-<element name="U$318" library="top" package="ZED#F9P#13" value="" x="52.578" y="115.189" smashed="yes" rot="MR90"/>
-<element name="U$319" library="top" package="0X4313" value="" x="53.848" y="120.777" smashed="yes" rot="MR90"/>
-<element name="U$320" library="top" package="0X4213" value="" x="52.578" y="120.777" smashed="yes" rot="MR90"/>
+<element name="U$316" library="top" package="DEF_ADDRESS#_12" value="" x="55.372" y="117.348" smashed="yes" rot="MR90"/>
+<element name="U$317" library="top" package="NEO#D9S#13" value="" x="54.102" y="115.062" smashed="yes" rot="MR90"/>
+<element name="U$318" library="top" package="ZED#F9P#13" value="" x="52.832" y="115.189" smashed="yes" rot="MR90"/>
+<element name="U$319" library="top" package="0X4313" value="" x="54.102" y="120.777" smashed="yes" rot="MR90"/>
+<element name="U$320" library="top" package="0X4213" value="" x="52.832" y="120.777" smashed="yes" rot="MR90"/>
 <element name="LOGO20" library="SparkFun-Aesthetics" package="QWIIC_5MM" value="QWIIC_LOGO_5MM" x="55.118" y="120.777" smashed="yes"/>
 <element name="E$1" library="SparkFun-Aesthetics" package="FIDUCIAL-1X2" value="" x="9.398" y="129.6035" smashed="yes"/>
